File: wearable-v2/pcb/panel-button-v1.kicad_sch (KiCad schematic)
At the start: 2 parts, among them J5 PNL_2_SOCKET, SW1 SW_Push

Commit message: Further V2 routing
Signed-off-by: Adam Fowler <adam@adamfowler.org>
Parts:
- SW1: footprint (none) -> Button_Switch_SMD:SW_Push_1P1T_NO_CK_KSC6xxJ
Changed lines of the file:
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@@
       (effects (font (size 1.27 1.27)))
     )
-    (property "Footprint" "" (at 116.84 35.56 0)
+    (property "Footprint" "Button_Switch_SMD:SW_Push_1P1T_NO_CK_KSC6xxJ" (at 116.84 35.56 0)
       (effects (font (size 1.27 1.27)) hide)
     )

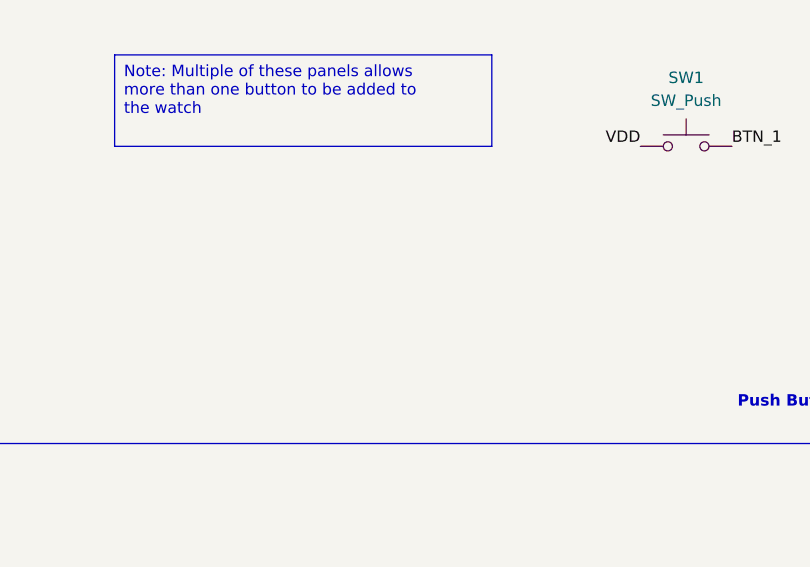
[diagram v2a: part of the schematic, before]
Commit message: Added I2C and I3C notes and additional resistors
Signed-off-by: Adam Fowler <adam@adamfowler.org>
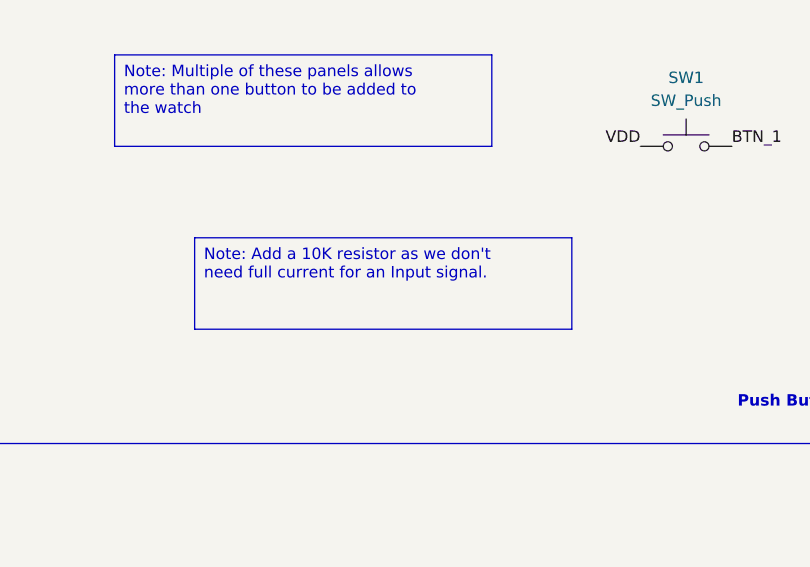
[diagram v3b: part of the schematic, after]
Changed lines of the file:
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@@
     (effects (font (size 1.27 1.27) (thickness 0.254) bold) (justify left top))
+  )
+  (text_box "Note: Add a 10K resistor as we don't need full current for an Input signal."
+    (at 62.23 50.8 0) (size 41.91 10.16)
+    (stroke (width 0) (type default))
+    (fill (type none))
+    (effects (font (size 1.27 1.27)) (justify left top))
   )
   (text_box "Note: Multiple of these panels allows more than one button to be added to the watch"
